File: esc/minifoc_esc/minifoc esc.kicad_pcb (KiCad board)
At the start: 4 copper layers, 18.4 x 14.3 mm, 16 parts, among them J1 Conn_02x09_Odd_Even, U1 DRV8316CRRGFR

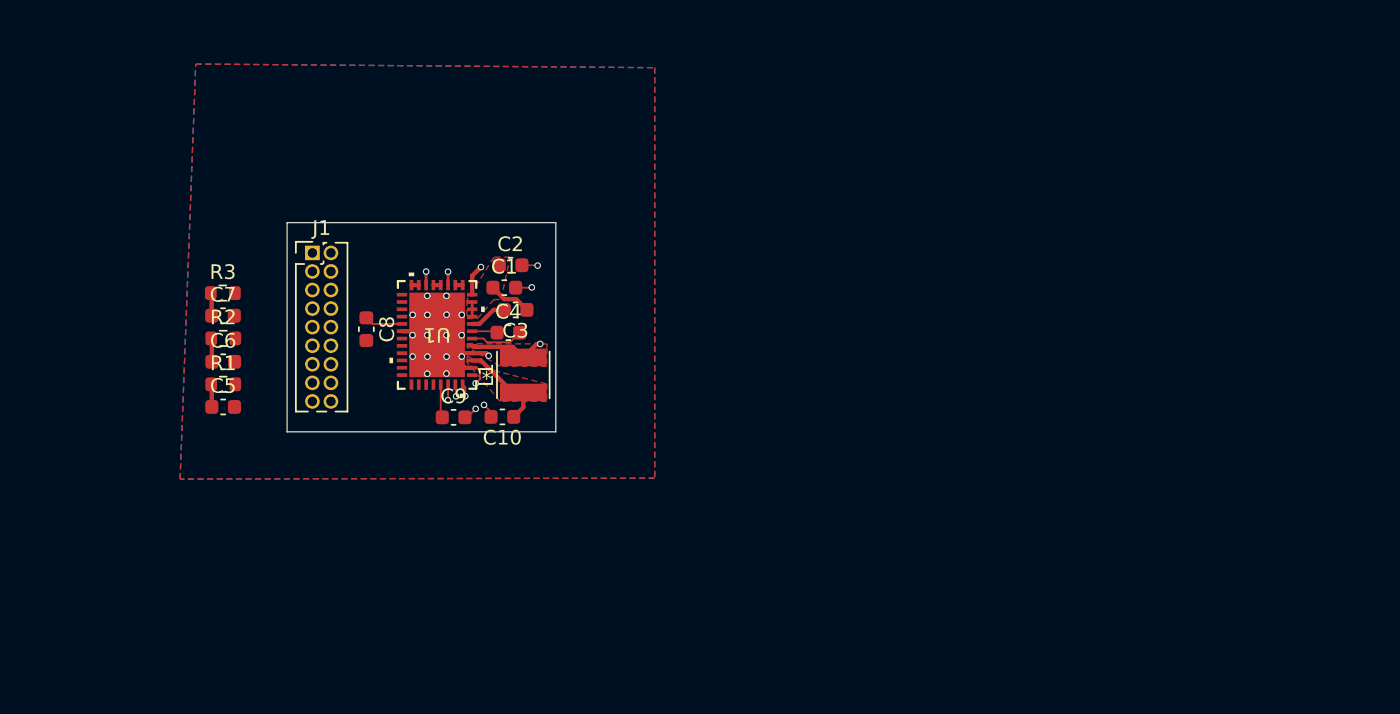
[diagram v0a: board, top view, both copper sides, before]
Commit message: Feat[minifoc_esc]: single-side PCB layout
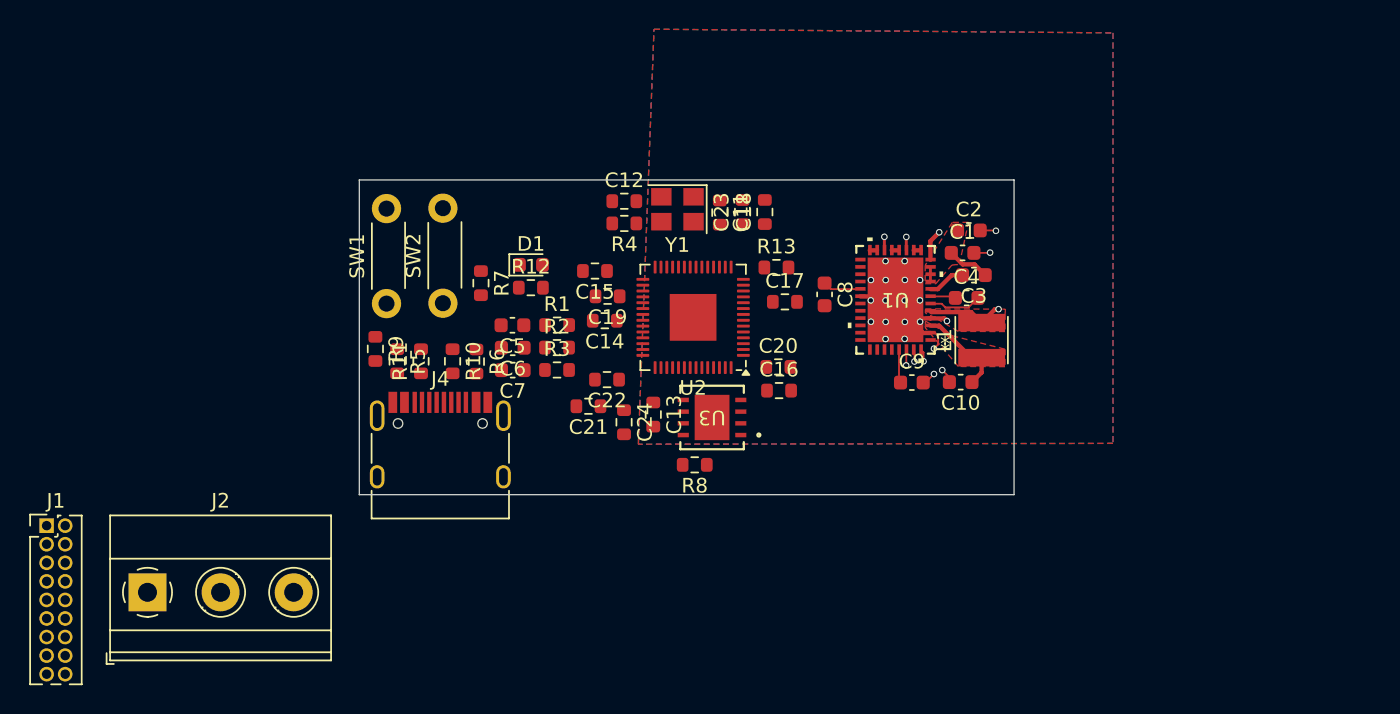
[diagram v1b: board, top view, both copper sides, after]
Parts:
- added C11: 27pF, Resistor_SMD:R_0603_1608Metric, F.Cu at (154.7, 102.4)
- added C12: 27pF, Resistor_SMD:R_0603_1608Metric, F.Cu at (148.1, 101.7)
- added C13: 1uF, Resistor_SMD:R_0603_1608Metric, F.Cu at (150.1, 116.3)
- added C14: 1uF, Resistor_SMD:R_0603_1608Metric, F.Cu at (146.8, 109.8)
- added C15: 0.1uF, Resistor_SMD:R_0603_1608Metric, F.Cu at (146.1, 106.4)
- added C16: 0.1uF, Resistor_SMD:R_0603_1608Metric, F.Cu at (158.7, 114.6)
- added C17: 0.1uF, Resistor_SMD:R_0603_1608Metric, F.Cu at (159.1, 108.5)
- added C18: 0.1uF, Resistor_SMD:R_0603_1608Metric, F.Cu at (157.7, 102.4)
- added C19: 0.1uF, Resistor_SMD:R_0603_1608Metric, F.Cu at (147.0, 108.2)
- added C20: 0.1uF, Resistor_SMD:R_0603_1608Metric, F.Cu at (158.7, 113.0)
- added C21: 0.1uF, Resistor_SMD:R_0603_1608Metric, F.Cu at (145.7, 115.7)
- added C22: 0.1uF, Resistor_SMD:R_0603_1608Metric, F.Cu at (146.9, 113.9)
- added C23: 0.1uF, Resistor_SMD:R_0603_1608Metric, F.Cu at (156.2, 102.4)
- added C24: 0.1uF, Resistor_SMD:R_0603_1608Metric, F.Cu at (148.1, 116.8)
- added D1: LED_Small, LED_SMD:LED_0603_1608Metric, F.Cu at (141.7, 106.0)
- added J2: Conn_01x03, TerminalBlock_Phoenix:TerminalBlock_Phoenix_MKDS-1,5-3_1x03_P5.00mm_Horizontal, F.Cu at (115.5, 128.4)
- added J4: USB_C_Receptacle_USB2.0_16P, Connector_USB:USB_C_Receptacle_HRO_TYPE-C-31-M-12, F.Cu at (135.5, 119.5)
- added R10: 27, Resistor_SMD:R_0603_1608Metric, F.Cu at (136.4, 112.6)
- added R11: 27, Resistor_SMD:R_0603_1608Metric, F.Cu at (134.2, 112.6)
- added R12: 2.7k, Resistor_SMD:R_0603_1608Metric, F.Cu at (141.7, 107.6)
- added R13: 10k, Resistor_SMD:R_0603_1608Metric, F.Cu at (158.5, 106.2)
- added R4: 1k, Resistor_SMD:R_0603_1608Metric, F.Cu at (148.1, 103.2)
- added R5: 5.1k, Resistor_SMD:R_0603_1608Metric, F.Cu at (132.6, 112.6)
- added R6: 5.1k, Resistor_SMD:R_0603_1608Metric, F.Cu at (138.0, 112.6)
- added R7: 1k, Resistor_SMD:R_0603_1608Metric, F.Cu at (138.3, 107.3)
- added R8: 10k, Resistor_SMD:R_0603_1608Metric, F.Cu at (152.9, 119.7)
- added R9: 1k, Resistor_SMD:R_0603_1608Metric, F.Cu at (131.1, 111.8)
- added SW1: RESET, SLIM_Switch:SW_PUSH_6mm_SLIM, F.Cu at (131.9, 108.7)
- added SW2: BOOT, SLIM_Switch:SW_PUSH_6mm_SLIM, F.Cu at (135.7, 108.6)
- added U2: RP2040, Package_DFN_QFN:QFN-56-1EP_7x7mm_P0.4mm_EP3.2x3.2mm, F.Cu at (152.8, 109.6)
- added U3: W25Q64JVXGIQ TR, DFN_XGIQ TR_WIN:DFN_XGIQ TR_WIN, F.Cu at (154.1, 116.5)
- added Y1: 12Mhz, Crystal:Crystal_SMD_3225-4Pin_3.2x2.5mm, F.Cu at (151.8, 102.2)
- moved U1 31.5 mm to (166.7, 108.4)
- moved C1 31.4 mm to (171.3, 105.2)
- moved C4 31.4 mm to (171.6, 108.3)
- moved C8 31.4 mm to (161.8, 108.0)
- moved C9 31.4 mm to (167.8, 114.1)
- moved C10 31.4 mm to (171.1, 114.0)
- moved C2 31.4 mm to (171.7, 103.7)
- moved C3 31.4 mm to (172.0, 106.7)
- moved L1 31.4 mm to (172.6, 111.2)
- moved J1 26.1 mm to (108.6, 123.9)
- moved R3 23.5 mm to (143.5, 113.2)
- moved R1 23.2 mm to (143.5, 110.1)
- moved R2 22.8 mm to (143.5, 111.7)
- moved C5 20.6 mm to (140.5, 110.1), turned to 180 degrees
- moved C7 20.2 mm to (140.5, 113.2), turned to 180 degrees
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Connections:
- net /OUTA renamed OUTA
- net /OUTB renamed OUTB
- net /OUTC renamed OUTC
- C5 pad 1: /ADC3 -> /SOA
- C6 pad 1: /ADC2 -> /SOB
- C7 pad 1: /ADC1 -> /SOC
- J1 pad 1: /INLC -> unconnected-(J1-Pin_1-Pad1)
- J1 pad 11: /INHA -> unconnected-(J1-Pin_11-Pad11)
- J1 pad 3: /INHC -> unconnected-(J1-Pin_3-Pad3)
- J1 pad 5: /INLB -> unconnected-(J1-Pin_5-Pad5)
- J1 pad 7: /INHB -> unconnected-(J1-Pin_7-Pad7)
- J1 pad 9: /INLA -> unconnected-(J1-Pin_9-Pad9)
- R1 pad 1: /ADC3 -> /SOA
- R2 pad 1: /ADC2 -> /SOB
- R3 pad 1: /ADC1 -> /SOC
- U1 pad 33: /SD0 -> /SDO
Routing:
- net /ADC2: track 1.62 -> 0.00 mm
- net /ADC1: track 1.57 -> 0.00 mm
- net /ADC3: track 1.57 -> 0.00 mm
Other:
- board size 18.4 x 14.3 mm -> 44.8 x 21.5 mm

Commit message: Fix[electrical]: resolve 8.99 pcb_text crash
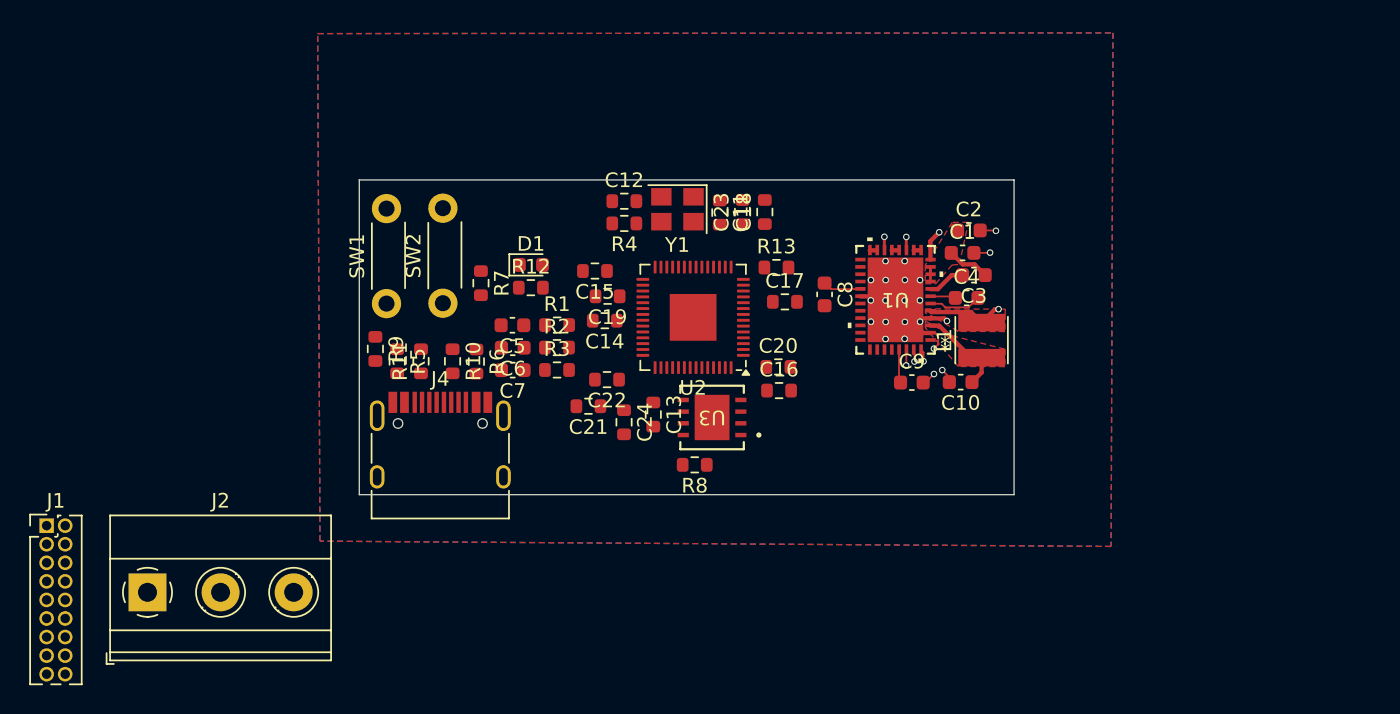
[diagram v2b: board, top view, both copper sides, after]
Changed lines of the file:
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@@
 		(tags "resistor")
 		(property "Reference" "C22"
-			(at 0 -1.43 360)
+			(at 0 -1.43 0)
 			(layer "F.SilkS")
 			(effects
@@
 		)
 		(property "Value" "0.1uF"
-			(at 0 1.43 360)
+			(at 0 1.43 0)
 			(layer "F.Fab")
 			(effects
@@
 		)
 		(fp_text user "${REFERENCE}"
-			(at 0 0 360)
+			(at 0 0 0)
 			(layer "F.Fab")
 			(effects
@@
 		(tags "resistor")
 		(property "Reference" "R4"
-			(at 0 -1.43 360)
+			(at 0 -1.43 0)
 			(layer "F.SilkS")
 			(effects
@@
 		)
 		(property "Value" "1k"
-			(at 0 1.43 360)
+			(at 0 1.43 0)
 			(layer "F.Fab")
 			(effects
@@
 		)
 		(fp_text user "${REFERENCE}"
-			(at 0 0 360)
+			(at 0 0 0)
 			(layer "F.Fab")
 			(effects
@@
 		(tags "capacitor")
 		(property "Reference" "C6"
-			(at 0 -1.43 360)
+			(at 0 -1.43 0)
 			(layer "F.SilkS")
 			(effects
@@
 		)
 		(property "Value" "30pF"
-			(at 0 1.43 360)
+			(at 0 1.43 0)
 			(layer "F.Fab")
 			(effects
@@
 		)
 		(fp_text user "${REFERENCE}"
-			(at 0 0 360)
+			(at 0 0 0)
 			(layer "F.Fab")
 			(effects
@@
 		(tags "resistor")
 		(property "Reference" "C19"
-			(at 0 -1.43 360)
+			(at 0 -1.43 0)
 			(layer "F.SilkS")
 			(effects
@@
 		)
 		(property "Value" "0.1uF"
-			(at 0 1.43 360)
+			(at 0 1.43 0)
 			(layer "F.Fab")
 			(effects
@@
 		)
 		(fp_text user "${REFERENCE}"
-			(at 0 0 360)
+			(at 0 0 0)
 			(layer "F.Fab")
 			(effects
@@
 		(tags "capacitor")
 		(property "Reference" "C5"
-			(at 0 -1.43 360)
+			(at 0 -1.43 0)
 			(layer "F.SilkS")
 			(effects
@@
 		)
 		(property "Value" "30pF"
-			(at 0 1.43 360)
+			(at 0 1.43 0)
 			(layer "F.Fab")
 			(effects
@@
 		)
 		(fp_text user "${REFERENCE}"
-			(at 0 0 360)
+			(at 0 0 0)
 			(layer "F.Fab")
 			(effects
@@
 		(tags "capacitor")
 		(property "Reference" "C7"
-			(at 0 -1.43 360)
+			(at 0 -1.43 0)
 			(layer "F.SilkS")
 			(effects
@@
 		)
 		(property "Value" "30pF"
-			(at 0 1.43 360)
+			(at 0 1.43 0)
 			(layer "F.Fab")
 			(effects
@@
 		)
 		(fp_text user "${REFERENCE}"
-			(at 0 0 360)
+			(at 0 0 0)
 			(layer "F.Fab")
 			(effects
@@
 		(tags "resistor")
 		(property "Reference" "R8"
-			(at 0 -1.43 360)
+			(at 0 -1.43 0)
 			(layer "F.SilkS")
 			(effects
@@
 		)
 		(property "Value" "10k"
-			(at 0 1.43 360)
+			(at 0 1.43 0)
 			(layer "F.Fab")
 			(effects
@@
 		)
 		(fp_text user "${REFERENCE}"
-			(at 0 0 360)
+			(at 0 0 0)
 			(layer "F.Fab")
 			(effects
@@
 		(tags "resistor")
 		(property "Reference" "C12"
-			(at 0 -1.43 360)
+			(at 0 -1.43 0)
 			(layer "F.SilkS")
 			(effects
@@
 		)
 		(property "Value" "27pF"
-			(at 0 1.43 360)
+			(at 0 1.43 0)
 			(layer "F.Fab")
 			(effects
@@
 		)
 		(fp_text user "${REFERENCE}"
-			(at 0 0 360)
+			(at 0 0 0)
 			(layer "F.Fab")
 			(effects
@@
 		)
 		(property "Footprint" "DFN_XGIQ TR_WIN:DFN_XGIQ TR_WIN"
-			(at 0 0 360)
+			(at 0 0 0)
 			(layer "F.Fab")
 			(hide yes)
@@
 		)
 		(property "Datasheet" "W25Q64JVXGIQ TR"
-			(at 0 0 360)
+			(at 0 0 0)
 			(layer "F.Fab")
 			(hide yes)
@@
 		)
 		(property "Description" ""
-			(at 0 0 360)
+			(at 0 0 0)
 			(layer "F.Fab")
 			(hide yes)
@@
 		(tags "usb usb-c 2.0 pd")
 		(property "Reference" "J4"
-			(at 0 -5.645 360)
+			(at 0 -5.645 0)
 			(layer "F.SilkS")
 			(effects
@@
 		)
 		(property "Value" "USB_C_Receptacle_USB2.0_16P"
-			(at 0 5.1 360)
+			(at 0 5.1 0)
 			(layer "F.Fab")
 			(effects
@@
 		)
 		(fp_text user "${REFERENCE}"
-			(at 0 0 360)
+			(at 0 0 0)
 			(layer "F.Fab")
 			(effects
@@
 		(tags "resistor")
 		(property "Reference" "C15"
-			(at 0 -1.43 360)
+			(at 0 -1.43 0)
 			(layer "F.SilkS")
 			(effects
@@
 		)
 		(property "Value" "0.1uF"
-			(at 0 1.43 360)
+			(at 0 1.43 0)
 			(layer "F.Fab")
 			(effects
@@
 		)
 		(fp_text user "${REFERENCE}"
-			(at 0 0 360)
+			(at 0 0 0)
 			(layer "F.Fab")
 			(effects
@@
 		)
 		(property "Footprint" "DRV8316C:VQFN40_RGF_TEX-L"
-			(at 0 0 360)
+			(at 0 0 0)
 			(layer "F.Fab")
 			(hide yes)
@@
 		)
 		(property "Datasheet" "DRV8316CRRGFR"
-			(at 0 0 360)
+			(at 0 0 0)
 			(layer "F.Fab")
 			(hide yes)
@@
 		)
 		(property "Description" ""
-			(at 0 0 360)
+			(at 0 0 0)
 			(layer "F.Fab")
 			(hide yes)
@@
 		)
 		(fp_text user "*"
-			(at -3.3909 -3.000756 360)
+			(at -3.3909 -3.000756 0)
 			(layer "F.SilkS")
 			(effects
@@
 		)
 		(fp_text user "*"
-			(at -2.0447 -3.000756 360)
+			(at -2.0447 -3.000756 0)
 			(layer "F.Fab")
 			(effects
@@
 		(tags "SMD SMT crystal")
 		(property "Reference" "Y1"
-			(at 0 -2.45 360)
+			(at 0 -2.45 0)
 			(layer "F.SilkS")
 			(effects
@@
 		)
 		(property "Value" "12Mhz"
-			(at 0 2.45 360)
+			(at 0 2.45 0)
 			(layer "F.Fab")
 			(effects
@@
 		)
 		(fp_text user "${REFERENCE}"
-			(at 0 0 360)
+			(at 0 0 0)
 			(layer "F.Fab")
 			(effects
@@
 		(tags "resistor")
 		(property "Reference" "C14"
-			(at 0 -1.43 360)
+			(at 0 -1.43 0)
 			(layer "F.SilkS")
 			(effects
@@
 		)
 		(property "Value" "1uF"
-			(at 0 1.43 360)
+			(at 0 1.43 0)
 			(layer "F.Fab")
 			(effects
@@
 		)
 		(fp_text user "${REFERENCE}"
-			(at 0 0 360)
+			(at 0 0 0)
 			(layer "F.Fab")
 			(effects
@@
 		(tags "resistor")
 		(property "Reference" "R13"
-			(at 0 -1.43 360)
+			(at 0 -1.43 0)
 			(layer "F.SilkS")
 			(effects
@@
 		)
 		(property "Value" "10k"
-			(at 0 1.43 360)
+			(at 0 1.43 0)
 			(layer "F.Fab")
 			(effects
@@
 		)
 		(fp_text user "${REFERENCE}"
-			(at 0 0 360)
+			(at 0 0 0)
 			(layer "F.Fab")
 			(effects
@@
 		(tags "resistor")
 		(property "Reference" "C21"
-			(at 0 -1.43 360)
+			(at 0 -1.43 0)
 			(layer "F.SilkS")
 			(effects
@@
 		)
 		(property "Value" "0.1uF"
-			(at 0 1.43 360)
+			(at 0 1.43 0)
 			(layer "F.Fab")
 			(effects
@@
 		)
 		(fp_text user "${REFERENCE}"
-			(at 0 0 360)
+			(at 0 0 0)
 			(layer "F.Fab")
 			(effects
@@
 	)
 	(gr_text "EDGE_CONN / B2B to MCU"
-		(at 155.38 117.24 90)
+		(at 146.42 95.09 0)
 		(layer "Cmts.User")
 		(effects
@@
 		(layer "Cmts.User")
 		(pts
-			(xy 174.79 115.06) (xy 156.41 115.06)
+			(xy 174.79 121.74) (xy 174.79 100.21)
 		)
-		(height 5.1)
-		(orientation 0)
-		(gr_text "18.3800 mm"
-			(at 165.6 119.01 0)
+		(height 4.12)
+		(orientation 1)
+		(gr_text "21.5300 mm"
+			(at 177.76 110.975 90)
 			(layer "Cmts.User")
 			(effects
@@
 		(layer "Cmts.User")
 		(pts
-			(xy 174.79 100.75) (xy 174.79 115.06)
+			(xy 174.79 121.74) (xy 129.998 121.74)
 		)
-		(height 4.95)
-		(orientation 1)
-		(gr_text "14.3100 mm"
-			(at 178.59 107.905 90)
+		(height 7.45)
+		(orientation 0)
+		(gr_text "44.7920 mm"
+			(at 152.394 128.04 0)
 			(layer "Cmts.User")
 			(effects
@@
 		(polygon
 			(pts
-				(xy 150.16 89.9) (xy 181.56 90.15) (xy 181.56 118.23) (xy 149.09 118.29)
+				(xy 127.15 90.2) (xy 181.56 90.15) (xy 181.43 125.28) (xy 127.31 124.92)
 			)
 		)

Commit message: Feat[minifoc_esc]: revised layout
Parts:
- removed J1: Conn_02x09_Odd_Even, Connector_PinHeader_1.27mm:PinHeader_2x09_P1.27mm_Vertical
- C21, C22: value 0.1uF -> 1uF
- moved J2 71.6 mm to (186.6, 119.6)
- moved R6 34.5 mm to (172.4, 115.8), turned to 180 degrees
- moved R10 33.1 mm to (169.4, 115.8), turned to 180 degrees
- moved J4 32.5 mm to (168.0, 121.8)
- moved R11 32.3 mm to (166.3, 115.7), turned to 180 degrees
- moved R5 30.9 mm to (163.3, 115.8), turned to 0 degrees
- moved SW2 19.4 mm to (149.9, 121.8), turned to 0 degrees
- moved R9 19.1 mm to (147.6, 121.4), turned to 90 degrees
- moved SW1 18.3 mm to (145.0, 121.4)
- moved R7 16.8 mm to (149.9, 119.5), turned to 180 degrees
- moved C14 11.6 mm to (154.6, 118.5)
- moved C18 10.9 mm to (159.8, 113.2), turned to 0 degrees
- moved C16 10.4 mm to (148.4, 115.5), turned to 180 degrees
- moved C23 8.75 mm to (148.4, 106.3), turned to 180 degrees
- moved C24 7.21 mm to (155.3, 116.2)
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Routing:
- net /FB_BK: track 6.35 -> 35.8 mm, vias 0 -> 1
- net GND: track 19.9 -> 48.9 mm, vias 25 -> 49
- net /RP2040/QSPI_CS: track 0.00 -> 12.1 mm
- net /RP2040/LED: track 0.00 -> 10.5 mm, vias 0 -> 2
- net /DRVOFF: track 0.00 -> 10.4 mm, vias 0 -> 2
- net /NSCS: track 0.00 -> 10.4 mm, vias 0 -> 2
- net /SCLK: track 0.00 -> 9.62 mm, vias 0 -> 2
- net /RP2040/+1.1V: track 0.00 -> 9.18 mm
- net /NFAULT: track 0.00 -> 8.90 mm, vias 0 -> 2
- net /RP2040/QSPI_SD1: track 0.00 -> 8.42 mm
- net /SDI: track 0.00 -> 8.41 mm
- net /NSLEEP: track 0.00 -> 7.91 mm
- net /SDO: track 0.00 -> 7.85 mm
- net /RP2040/QSPI_SD2: track 0.00 -> 7.69 mm
- net /INLA: track 0.00 -> 7.23 mm
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- added copper zone on F.Cu, net OUTA
- added copper zone on F.Cu, net OUTB
- added copper zone on F.Cu, net OUTC
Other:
- board size 44.8 x 21.5 mm -> 31.6 x 23.8 mm
- board text added: "Test points, debugging interfaces?"
- board text removed: "EDGE_CONN / B2B to MCU"
